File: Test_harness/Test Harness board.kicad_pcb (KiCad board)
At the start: 4 copper layers, 233 x 160 mm, 131 parts, among them U1 TCA9548APWR

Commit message: route the left connector of test_harness board
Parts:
- CL1, CL1_1, CL1_2, CL2, CL2_1, CL2_2, CL3, CL3_1, CL3_2, CL4, CL4_1, CL4_2, CL5, CL5_1, CL5_2: footprint Capacitor_SMD:C_1206_3216Metric -> Capacitor_SMD:C_0805_2012Metric
- J_LEFT1: value DIN_41612_C-96 -> DIN_41612_R-96-Female
- moved CL2_1 277.9 mm to (130.9, 138.8)
- moved D_A0 274.7 mm to (99.4, -70.6)
- moved D_A1 274.7 mm to (17.2, -27.2)
- moved D_A10 274.7 mm to (138.5, -101.1)
- moved D_A11 274.7 mm to (11.2, -27.2)
- moved D_A13 274.7 mm to (62.8, -66.1)
- moved D_A14 274.7 mm to (99.4, -60.7)
- moved D_A15 274.7 mm to (46.5, -28.4)
- moved D_A16 274.7 mm to (87.8, -50.9)
- moved D_A17 274.7 mm to (75.8, -56.9)
- moved D_A18 274.7 mm to (126.2, -86.8)
- moved D_A19 274.7 mm to (86.7, -73.7)
- moved D_A2 274.7 mm to (70.7, -34.7)
- moved D_A20 274.7 mm to (98.8, -73.9)
- moved D_A21 274.7 mm to (70.7, -38.0)
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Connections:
- UL5 pad 15: +5V -> GND
- UL5 pad 17: GND -> +5V
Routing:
- net GND: track 0.00 -> 261.5 mm, vias 0 -> 19
- net +5V: track 0.00 -> 132.2 mm, vias 0 -> 18
- net /Left connector/SCL: track 0.00 -> 100.4 mm, vias 0 -> 4
- net /Left connector/SDA: track 0.00 -> 97.1 mm, vias 0 -> 4
- net /Left connector/A2: track 35.9 -> 98.5 mm, vias 3 -> 4
- net /Left connector/A0: track 34.3 -> 96.0 mm, vias 3 -> 4
- net /Left connector/A18: track 40.2 -> 99.9 mm, vias 2 -> 4
- net /Left connector/A19: track 43.2 -> 101.1 mm, vias 2 -> 4
- net /Left connector/A3: track 36.8 -> 94.0 mm, vias 3 -> 4
- net /Left connector/A14: track 29.7 -> 86.5 mm, vias 2 -> 4
- net /Left connector/A20: track 45.7 -> 102.4 mm, vias 2 -> 4
- net /Left connector/A1: track 35.2 -> 91.4 mm, vias 3 -> 4
- net /Left connector/A21: track 48.4 -> 103.6 mm, vias 2 -> 4
- net /Left connector/A15: track 32.3 -> 86.4 mm, vias 2 -> 4
- net /Left connector/A16: track 35.0 -> 89.0 mm, vias 2 -> 4
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
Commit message: the left connector side of the test harness is in good shape.. even discovered that we can have those HP displays now made by broadcom
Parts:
- added DSP_A0: HDSP-0762, Components:HDSP-076x-077x-086x-096x, F.Cu at (122.7, 106.0)
- added DSP_A1: HDSP-0762, Components:HDSP-076x-077x-086x-096x, F.Cu at (112.6, 106.0)
- added DSP_A2: HDSP-0762, Components:HDSP-076x-077x-086x-096x, F.Cu at (102.4, 106.0)
- added DSP_A3: HDSP-0762, Components:HDSP-076x-077x-086x-096x, F.Cu at (92.3, 106.0)
- added DSP_A4: HDSP-0762, Components:HDSP-076x-077x-086x-096x, F.Cu at (82.1, 106.0)
- added DSP_A5: HDSP-0762, Components:HDSP-076x-077x-086x-096x, F.Cu at (71.9, 106.0)
- added DSP_D0: HDSP-0762, Components:HDSP-076x-077x-086x-096x, F.Cu at (51.5, 106.0)
- added DSP_D1: HDSP-0762, Components:HDSP-076x-077x-086x-096x, F.Cu at (41.4, 106.0)
- added DSP_L0: HDSP-0762, Components:HDSP-076x-077x-086x-096x, F.Cu at (71.9, 71.3)
- added DSP_L1: HDSP-0762, Components:HDSP-076x-077x-086x-096x, F.Cu at (41.4, 71.3)
- added DSP_L2: HDSP-0762, Components:HDSP-076x-077x-086x-096x, F.Cu at (61.7, 71.3)
- added DSP_L3: HDSP-0762, Components:HDSP-076x-077x-086x-096x, F.Cu at (51.5, 71.3)
- moved RNL5_2_1 296.8 mm to (256.3, 170.0)
- moved D__WR1 287.3 mm to (248.5, 170.7)
- moved D__RESET1 281.1 mm to (240.0, 172.6)
- moved D_IR2 272.6 mm to (236.6, 168.6)
- moved RNL5_1_1 272.4 mm to (225.9, 164.6)
- moved D_MEMORY1 267.8 mm to (243.1, 147.3)
- moved D_MEMREF1 265.6 mm to (232.1, 155.7)
- moved RNL5_2_2 261.4 mm to (218.7, 155.9)
- moved D_XL_MDR_HI1 257.3 mm to (237.3, 164.7)
- moved D_IR3 256.4 mm to (238.5, 156.7)
- moved RNL5_1_2 256.2 mm to (224.6, 147.1)
- moved D__IR1 254.8 mm to (246.9, 140.8)
- moved D__STOP_CLK1 254.5 mm to (233.7, 150.5)
- moved D_XL_MDR_LO1 252.1 mm to (232.6, 160.0)
- moved D__PSEL1 249.6 mm to (245.2, 151.4)
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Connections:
- RNL1_1_1 pad 5: Net-(D_L8-Pad1) -> Net-(D_L11-Pad1)
- RNL1_1_1 pad 6: Net-(D_L9-Pad1) -> Net-(D_L10-Pad1)
- RNL1_1_1 pad 7: Net-(D_L10-Pad1) -> Net-(D_L9-Pad1)
- RNL1_1_1 pad 8: Net-(D_L11-Pad1) -> Net-(D_L8-Pad1)
- RNL1_1_2 pad 5: Net-(D_L12-Pad1) -> Net-(D_L15-Pad1)
- RNL1_1_2 pad 6: Net-(D_L13-Pad1) -> Net-(D_L14-Pad1)
- RNL1_1_2 pad 7: Net-(D_L14-Pad1) -> Net-(D_L13-Pad1)
- RNL1_1_2 pad 8: Net-(D_L15-Pad1) -> Net-(D_L12-Pad1)
- RNL1_2_1 pad 5: Net-(D_L0-Pad1) -> Net-(D_L3-Pad1)
- RNL1_2_1 pad 6: Net-(D_L1-Pad1) -> Net-(D_L2-Pad1)
- RNL1_2_1 pad 7: Net-(D_L2-Pad1) -> Net-(D_L1-Pad1)
- RNL1_2_1 pad 8: Net-(D_L3-Pad1) -> Net-(D_L0-Pad1)
- RNL1_2_2 pad 5: Net-(D_L4-Pad1) -> Net-(D_L7-Pad1)
- RNL1_2_2 pad 6: Net-(D_L5-Pad1) -> Net-(D_L6-Pad1)
- RNL1_2_2 pad 7: Net-(D_L6-Pad1) -> Net-(D_L5-Pad1)
- RNL1_2_2 pad 8: Net-(D_L7-Pad1) -> Net-(D_L4-Pad1)
- RNL3_1_1 pad 5: Net-(D_A14-Pad1) -> Net-(D_A17-Pad1)
- RNL3_1_1 pad 6: Net-(D_A15-Pad1) -> Net-(D_A16-Pad1)
- RNL3_1_1 pad 7: Net-(D_A16-Pad1) -> Net-(D_A15-Pad1)
- RNL3_1_1 pad 8: Net-(D_A17-Pad1) -> Net-(D_A14-Pad1)
- RNL3_1_2 pad 5: Net-(D_A18-Pad1) -> Net-(D_A21-Pad1)
- RNL3_1_2 pad 6: Net-(D_A19-Pad1) -> Net-(D_A20-Pad1)
- RNL3_1_2 pad 7: Net-(D_A20-Pad1) -> Net-(D_A19-Pad1)
- RNL3_1_2 pad 8: Net-(D_A21-Pad1) -> Net-(D_A18-Pad1)
- RNL3_2_1 pad 5: Net-(D_A6-Pad1) -> Net-(D_A9-Pad1)
- RNL3_2_1 pad 6: Net-(D_A7-Pad1) -> Net-(D_A8-Pad1)
- RNL3_2_1 pad 7: Net-(D_A8-Pad1) -> Net-(D_A7-Pad1)
- RNL3_2_1 pad 8: Net-(D_A9-Pad1) -> Net-(D_A6-Pad1)
- RNL3_2_2 pad 5: Net-(D_A10-Pad1) -> Net-(D_A13-Pad1)
- RNL3_2_2 pad 6: Net-(D_A11-Pad1) -> Net-(D_A12-Pad1)
- RNL3_2_2 pad 7: Net-(D_A12-Pad1) -> Net-(D_A11-Pad1)
- RNL3_2_2 pad 8: Net-(D_A13-Pad1) -> Net-(D_A10-Pad1)
- RNL4_1_1 pad 7: Net-(D_A0-Pad1) -> Net-(D_A1-Pad1)
- RNL4_1_1 pad 8: Net-(D_A1-Pad1) -> Net-(D_A0-Pad1)
- RNL4_1_2 pad 5: Net-(D_A2-Pad1) -> Net-(D_A5-Pad1)
- RNL4_1_2 pad 6: Net-(D_A3-Pad1) -> Net-(D_A4-Pad1)
- RNL4_1_2 pad 7: Net-(D_A4-Pad1) -> Net-(D_A3-Pad1)
- RNL4_1_2 pad 8: Net-(D_A5-Pad1) -> Net-(D_A2-Pad1)
- RNL4_2_1 pad 5: Net-(D_D0-Pad1) -> Net-(D_D3-Pad1)
- RNL4_2_1 pad 6: Net-(D_D1-Pad1) -> Net-(D_D2-Pad1)
- RNL4_2_1 pad 7: Net-(D_D2-Pad1) -> Net-(D_D1-Pad1)
- RNL4_2_1 pad 8: Net-(D_D3-Pad1) -> Net-(D_D0-Pad1)
- RNL4_2_2 pad 5: Net-(D_D4-Pad1) -> Net-(D_D7-Pad1)
- RNL4_2_2 pad 6: Net-(D_D5-Pad1) -> Net-(D_D6-Pad1)
- RNL4_2_2 pad 7: Net-(D_D6-Pad1) -> Net-(D_D5-Pad1)
- RNL4_2_2 pad 8: Net-(D_D7-Pad1) -> Net-(D_D4-Pad1)
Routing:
- net /Left connector/D_MAR15: track 0.00 -> 85.9 mm, vias 0 -> 2
- net /Left connector/D_L0: track 0.00 -> 85.3 mm, vias 0 -> 2
- net /Left connector/D_L1: track 0.00 -> 81.5 mm, vias 0 -> 2
- net /Left connector/D_MAR14: track 0.00 -> 81.4 mm, vias 0 -> 3
- net /Left connector/D_L2: track 0.00 -> 77.7 mm, vias 0 -> 2
- net /Left connector/D_L4: track 0.00 -> 77.5 mm, vias 0 -> 2
- net /Left connector/D_MAR13: track 0.00 -> 76.9 mm, vias 0 -> 3
- net /Left connector/D_L15: track 0.00 -> 75.6 mm, vias 0 -> 2
- net /Left connector/D_L3: track 0.00 -> 74.2 mm, vias 0 -> 2
- net /Left connector/D_L5: track 0.00 -> 73.4 mm, vias 0 -> 2
- net /Left connector/D_MAR12: track 0.00 -> 72.0 mm, vias 0 -> 3
- net /Left connector/D_MAR11: track 0.00 -> 71.8 mm, vias 0 -> 2
- net /Left connector/D_L14: track 0.00 -> 70.7 mm, vias 0 -> 2
- net /Left connector/D_L6: track 0.00 -> 69.7 mm, vias 0 -> 2
- net /Left connector/D_MAR10: track 0.00 -> 67.5 mm, vias 0 -> 2
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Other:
- board text added: "ALU Left Bus"
- board text added: "Address Bus"
- board text added: "Data Bus"
- board text added: "Mem. Access Register"

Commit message: added a bunch of things, including board under test power control
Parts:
- added CBP1: 1µF, Capacitor_SMD:C_0805_2012Metric, F.Cu at (132.9, 142.4)
- added CBP2: 0.1µF, Capacitor_SMD:C_0805_2012Metric, F.Cu at (139.6, 144.7)
- added CBP3: 120µF, Capacitor_SMD:CP_Elec_6.3x9.9, F.Cu at (141.4, 150.5)
- added CDSP_A0: C_Small, Capacitor_SMD:C_0805_2012Metric, F.Cu at (122.8, 111.1)
- added CDSP_A1: C_Small, Capacitor_SMD:C_0805_2012Metric, F.Cu at (112.6, 111.1)
- added CDSP_A2: C_Small, Capacitor_SMD:C_0805_2012Metric, F.Cu at (102.4, 111.1)
- added CDSP_A3: C_Small, Capacitor_SMD:C_0805_2012Metric, F.Cu at (92.3, 111.1)
- added CDSP_A4: C_Small, Capacitor_SMD:C_0805_2012Metric, F.Cu at (82.1, 111.1)
- added CDSP_A5: C_Small, Capacitor_SMD:C_0805_2012Metric, F.Cu at (72.0, 111.1)
- added CDSP_D0: C_Small, Capacitor_SMD:C_0805_2012Metric, F.Cu at (51.5, 111.1)
- added CDSP_D1: C_Small, Capacitor_SMD:C_0805_2012Metric, F.Cu at (41.4, 111.1)
- added CDSP_L0: C_Small, Capacitor_SMD:C_0805_2012Metric, F.Cu at (71.9, 76.3)
- added CDSP_L1: C_Small, Capacitor_SMD:C_0805_2012Metric, F.Cu at (61.7, 76.3)
- added CDSP_L2: C_Small, Capacitor_SMD:C_0805_2012Metric, F.Cu at (51.5, 76.3)
- added CDSP_L3: C_Small, Capacitor_SMD:C_0805_2012Metric, F.Cu at (41.4, 76.3)
- added CDSP_MAR0: C_Small, Capacitor_SMD:C_0805_2012Metric, F.Cu at (128.7, 76.3)
- added CDSP_MAR1: C_Small, Capacitor_SMD:C_0805_2012Metric, F.Cu at (118.5, 76.3)
- added CDSP_MAR2: C_Small, Capacitor_SMD:C_0805_2012Metric, F.Cu at (108.3, 76.3)
- added CDSP_MAR3: C_Small, Capacitor_SMD:C_0805_2012Metric, F.Cu at (98.2, 76.3)
- added DBP1: LED_Small, LED_SMD:LED_0805_2012Metric, F.Cu at (144.4, 140.1)
- added DSP_MAR0: HDSP-0762, Components:HDSP-076x-077x-086x-096x, F.Cu at (118.5, 71.3)
- added DSP_MAR1: HDSP-0762, Components:HDSP-076x-077x-086x-096x, F.Cu at (128.7, 71.3)
- added DSP_MAR2: HDSP-0762, Components:HDSP-076x-077x-086x-096x, F.Cu at (108.3, 71.3)
- added DSP_MAR3: HDSP-0762, Components:HDSP-076x-077x-086x-096x, F.Cu at (98.2, 71.3)
- added RBP1: 10kΩ, Resistor_SMD:R_0805_2012Metric, F.Cu at (139.6, 135.8)
- added RBP2: 1kΩ, Resistor_SMD:R_0805_2012Metric, F.Cu at (144.4, 144.7)
- added RBP3: 1kΩ, Resistor_SMD:R_0805_2012Metric, F.Cu at (139.5, 131.0)
- added UBP1: AP22814AW5, Package_TO_SOT_SMD:SOT-23-5, F.Cu at (137.5, 140.1)
- moved RNL2_2_1 73.8 mm to (138.4, 84.2), turned to -90 degrees
- moved RNL2_1_1 55.3 mm to (111.7, 84.2), turned to -90 degrees
- moved RNL2_2_2 54.2 mm to (125.0, 84.2), turned to -90 degrees
- moved RNL2_1_2 43.0 mm to (98.4, 84.2), turned to -90 degrees
- moved RNL3_1_2 1.17 mm to (72.1, 118.3)
- moved RNL3_1_1 1.03 mm to (85.4, 118.3)
- moved RNL3_2_1 0.97 mm to (112.0, 118.3)
- moved RNL3_2_2 0.97 mm to (98.7, 118.3)
- moved RNL4_1_1 0.97 mm to (134.8, 118.3)
- moved RNL4_1_2 0.97 mm to (125.4, 118.3)
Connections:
- A1 pad 5: Net-(A1-Pad5) -> /PWR_BOARD_ON
- J_LEFT1 pad a32: +5V -> BRD_POWER
- J_LEFT1 pad b1: +5V -> BRD_POWER
- J_LEFT1 pad b11: +5V -> BRD_POWER
- J_LEFT1 pad b13: +5V -> BRD_POWER
- J_LEFT1 pad b17: +5V -> BRD_POWER
- J_LEFT1 pad b21: +5V -> BRD_POWER
- J_LEFT1 pad b24: +5V -> BRD_POWER
- J_LEFT1 pad b27: +5V -> BRD_POWER
- J_LEFT1 pad b32: +5V -> BRD_POWER
- J_LEFT1 pad c32: +5V -> BRD_POWER
- RNL2_1_1 pad 5: Net-(D_MAR8-Pad1) -> Net-(D_MAR11-Pad1)
- RNL2_1_1 pad 6: Net-(D_MAR9-Pad1) -> Net-(D_MAR10-Pad1)
- RNL2_1_1 pad 7: Net-(D_MAR10-Pad1) -> Net-(D_MAR9-Pad1)
- RNL2_1_1 pad 8: Net-(D_MAR11-Pad1) -> Net-(D_MAR8-Pad1)
- RNL2_1_2 pad 5: Net-(D_MAR12-Pad1) -> Net-(D_MAR15-Pad1)
- RNL2_1_2 pad 6: Net-(D_MAR13-Pad1) -> Net-(D_MAR14-Pad1)
- RNL2_1_2 pad 7: Net-(D_MAR14-Pad1) -> Net-(D_MAR13-Pad1)
- RNL2_1_2 pad 8: Net-(D_MAR15-Pad1) -> Net-(D_MAR12-Pad1)
- RNL2_2_1 pad 5: Net-(D_MAR0-Pad1) -> Net-(D_MAR3-Pad1)
- RNL2_2_1 pad 6: Net-(D_MAR1-Pad1) -> Net-(D_MAR2-Pad1)
- RNL2_2_1 pad 7: Net-(D_MAR2-Pad1) -> Net-(D_MAR1-Pad1)
- RNL2_2_1 pad 8: Net-(D_MAR3-Pad1) -> Net-(D_MAR0-Pad1)
- RNL2_2_2 pad 5: Net-(D_MAR4-Pad1) -> Net-(D_MAR7-Pad1)
- RNL2_2_2 pad 6: Net-(D_MAR5-Pad1) -> Net-(D_MAR6-Pad1)
- RNL2_2_2 pad 7: Net-(D_MAR6-Pad1) -> Net-(D_MAR5-Pad1)
- RNL2_2_2 pad 8: Net-(D_MAR7-Pad1) -> Net-(D_MAR4-Pad1)
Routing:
- net GND: track 278.6 -> 382.9 mm, vias 26 -> 33
- net /Left connector/D_XL_MDR_HI: track 0.00 -> 62.1 mm, vias 0 -> 2
- net /Left connector/D__PSEL1: track 0.00 -> 61.9 mm, vias 0 -> 2
- net /Left connector/D__RD: track 0.00 -> 60.6 mm, vias 0 -> 2
- net /Left connector/D_IR3: track 0.00 -> 60.4 mm, vias 0 -> 2
- net /Left connector/D_IR2: track 0.00 -> 58.8 mm, vias 0 -> 2
- net /Left connector/D__WR: track 0.00 -> 58.7 mm, vias 0 -> 2
- net /Left connector/D_IR1: track 0.00 -> 57.2 mm, vias 0 -> 2
- net /Left connector/D_XL_MDR_LO: track 0.00 -> 57.0 mm, vias 0 -> 2
- net /Left connector/D_MEMREF: track 0.00 -> 54.8 mm, vias 0 -> 2
- net /Left connector/D_MEMORY: track 0.00 -> 53.3 mm, vias 0 -> 2
- net /Left connector/D_A4: track 47.9 -> 97.8 mm, vias 0 -> 2
- net /Left connector/D__RESET: track 0.00 -> 49.8 mm, vias 0 -> 2
- net /Left connector/D_A2: track 49.8 -> 98.6 mm, vias 0 -> 2
- net /Left connector/D__STOP_CLK: track 0.00 -> 48.3 mm, vias 0 -> 2
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- added copper zone on F.Cu, net BRD_POWER
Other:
- board text added: "A0"
- board text added: "A1"
- board text added: "A2"
- board text added: "A3"
- board text added: "A4"
- board text added: "A5"
- board text added: "D0"
- board text added: "D1"
- board text added: "L0"
- board text added: "L1"
- board text added: "L2"
- board text added: "L3"
- board text added: "M0"
- board text added: "M1"
- board text added: "M2"
- board text added: "M3"

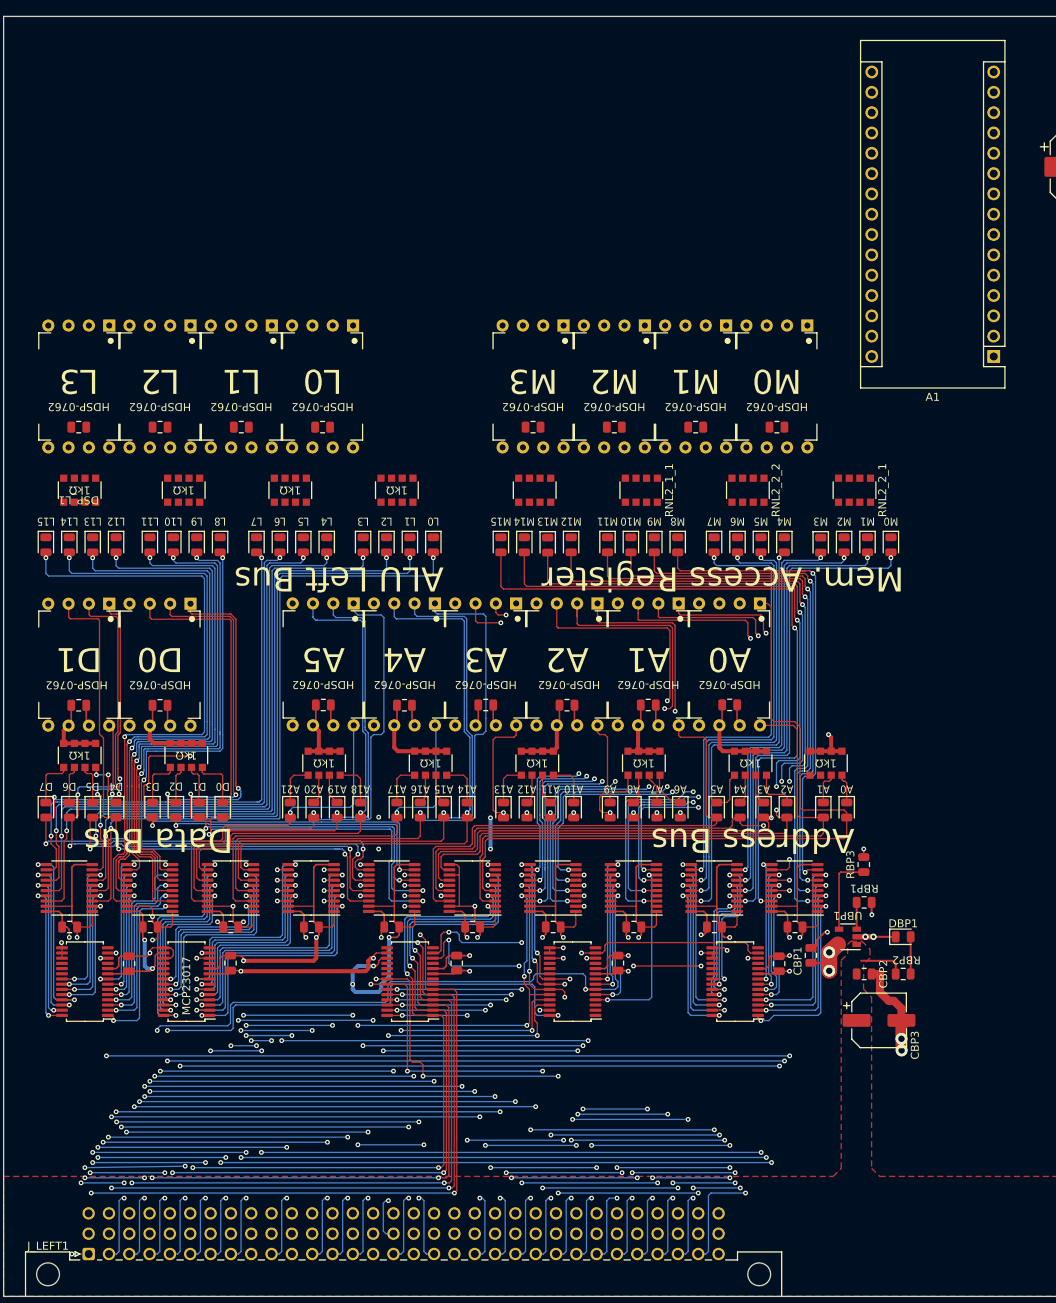
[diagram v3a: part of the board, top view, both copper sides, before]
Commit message: fix stuff, add series resistor on clock line ohms)
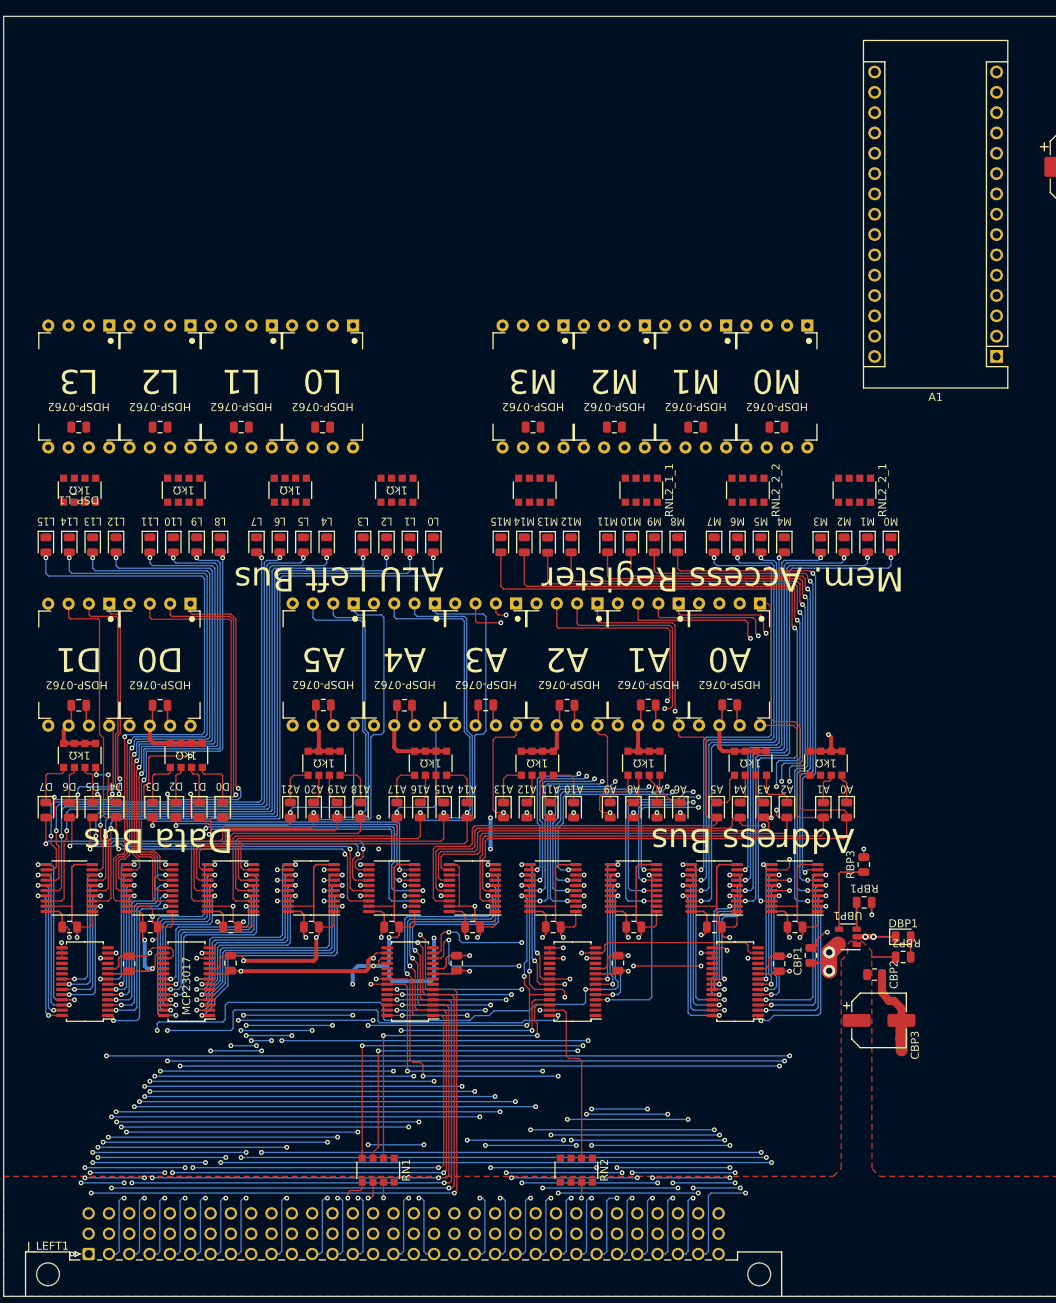
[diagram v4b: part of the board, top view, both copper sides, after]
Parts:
- added RN1: 82Ω, Resistor_SMD:R_Array_Convex_4x1206, F.Cu at (78.8, 169.2)
- added RN2: 82Ω, Resistor_SMD:R_Array_Convex_4x1206, F.Cu at (103.6, 169.2)
- moved DSP_MAR0 10.2 mm to (128.7, 71.3)
- moved DSP_MAR1 10.2 mm to (118.5, 71.3)
- moved RBP2 2.13 mm to (144.4, 142.6)
- moved CBP2 1.30 mm to (140.9, 144.8)
- moved A1 0.36 mm to (156.1, 67.5)
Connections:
- UL5 pad 26: /Left connector/_WR -> /Left connector/_rWR
- UL5 pad 27: /Left connector/_RD -> /Left connector/_rRD
- UL5 pad 7: /Left connector/_RESET -> /Left connector/_rRESET
- UL5 pad 8: /Left connector/_STOP_CLK -> /Left connector/_rSTOP_CLK
- UL5_1 pad 11: /Left connector/_STOP_CLK -> /Left connector/_rSTOP_CLK
- UL5_1 pad 13: /Left connector/_RESET -> /Left connector/_rRESET
- UL5_2 pad 4: /Left connector/_RD -> /Left connector/_rRD
- UL5_2 pad 6: /Left connector/_WR -> /Left connector/_rWR
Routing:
- net /Left connector/_RESET: track 82.0 -> 9.46 mm, vias 4 -> 1
- net /Left connector/_rRESET: track 0.00 -> 72.6 mm, vias 0 -> 4
- net /Left connector/_STOP_CLK: track 79.0 -> 8.41 mm, vias 4 -> 1
- net /Left connector/_rSTOP_CLK: track 0.00 -> 69.4 mm, vias 0 -> 4
- net /Left connector/_WR: track 76.3 -> 7.51 mm, vias 4 -> 1
- net /Left connector/_rWR: track 0.00 -> 65.4 mm, vias 0 -> 3
- net /Left connector/_RD: track 55.6 -> 9.05 mm, vias 2 -> 1
- net /Left connector/_rRD: track 0.00 -> 43.2 mm, vias 0 -> 2
- net GND: track 382.9 -> 378.5 mm, vias 33 -> 32
- net /Left connector/_PSEL1: track 105.9 -> 101.6 mm
- net +5V: track 153.1 -> 148.9 mm
- net BRD_POWER: track 5.76 -> 3.04 mm
- net /Left connector/XL_MDR_HI: track 77.3 -> 74.7 mm
- net Net-(DBP1-Pad2): track 4.65 -> 2.52 mm
- net /Left connector/D_D4: track 75.0 -> 73.3 mm
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
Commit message: fix lots of tiny details
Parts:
- moved D_MEMORY1 186.4 mm to (98.9, 29.2)
- moved D_MEMREF1 186.4 mm to (87.9, 37.5)
- moved D_XL_MDR_HI1 186.4 mm to (93.1, 46.6)
- moved D_XL_MDR_LO1 186.4 mm to (88.4, 41.9)
- moved D__IR1 186.4 mm to (102.8, 22.7)
- moved D__PSEL1 186.4 mm to (101.0, 33.3)
- moved D__RD1 186.4 mm to (88.7, 27.8)
- moved D__RESET1 186.4 mm to (95.8, 54.4)
- moved D__STOP_CLK1 186.4 mm to (89.5, 32.3)
- moved D__WR1 186.4 mm to (104.4, 52.5)
- moved RNL5_1_1 186.4 mm to (81.7, 46.5)
- moved RNL5_1_2 186.4 mm to (80.4, 29.0)
- moved RNL5_2_2 186.4 mm to (74.6, 37.7)
- moved D_IR2 186.4 mm to (92.4, 50.5)
- moved D_IR3 186.4 mm to (94.3, 38.6)
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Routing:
- net GND: track 378.5 -> 447.4 mm, vias 32 -> 35
- net /Left connector/D_MAR0: track 61.9 -> 102.3 mm
- net /Left connector/D_L13: track 66.3 -> 104.9 mm, vias 2 -> 3
- net /Left connector/D_L8: track 52.1 -> 89.7 mm, vias 2 -> 3
- net /Left connector/D_MAR1: track 57.6 -> 94.8 mm
- net /Left connector/D_L12: track 62.6 -> 99.1 mm, vias 2 -> 3
- net /Left connector/D_L14: track 70.5 -> 106.1 mm
- net /Left connector/D_L10: track 60.7 -> 94.5 mm
- net /Left connector/D_MAR2: track 53.4 -> 85.5 mm
- net /Left connector/D_L9: track 56.6 -> 88.3 mm, vias 2 -> 3
- net /Left connector/D_L15: track 75.1 -> 96.1 mm
- net /Left connector/D_L11: track 65.0 -> 83.4 mm, vias 2 -> 3
- net /Left connector/D_MAR3: track 49.2 -> 65.6 mm
- net +5V: track 148.9 -> 159.3 mm
- net /Left connector/D_MEMORY: track 53.3 -> 44.2 mm, vias 2 -> 3
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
